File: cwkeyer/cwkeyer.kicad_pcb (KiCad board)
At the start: 2 copper layers, 19 x 17.8 mm, 7 parts, among them J1 Conn_01x05, J2 Conn_01x03, Q1 S8050, U1 ATtiny85-20SU

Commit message: Change R1 from 1K to 4.7K
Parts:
- R1: value 1K -> 4.7K
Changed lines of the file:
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@@
       (effects (font (size 1 1) (thickness 0.15)))
     )
-    (fp_text value 1K (at 0 1.65 90) (layer F.Fab)
+    (fp_text value 4.7K (at 0 1.65 90) (layer F.Fab)
       (effects (font (size 1 1) (thickness 0.15)))
     )

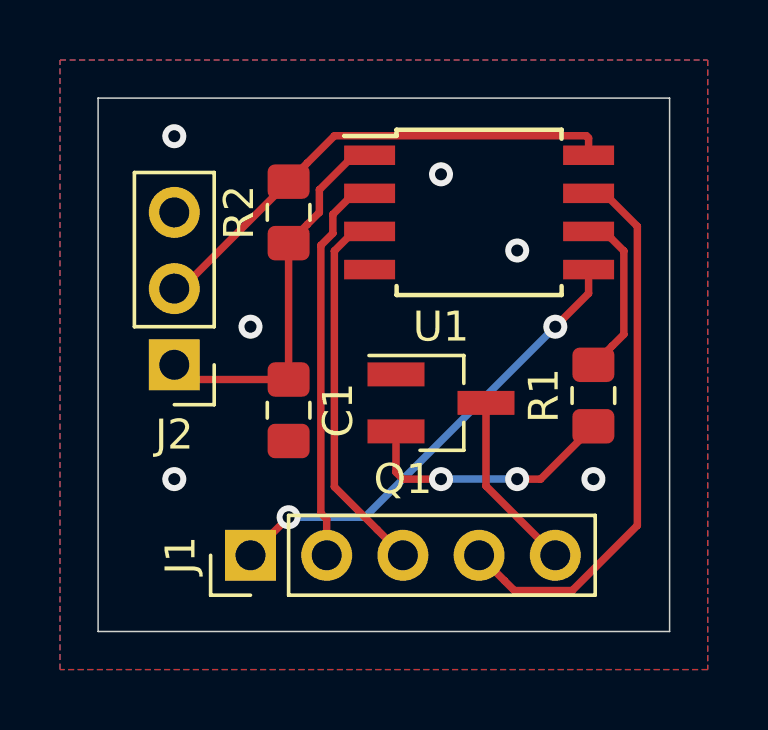
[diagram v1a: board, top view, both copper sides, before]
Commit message: Add C2 between VCC and GND. Reroute the PCB.
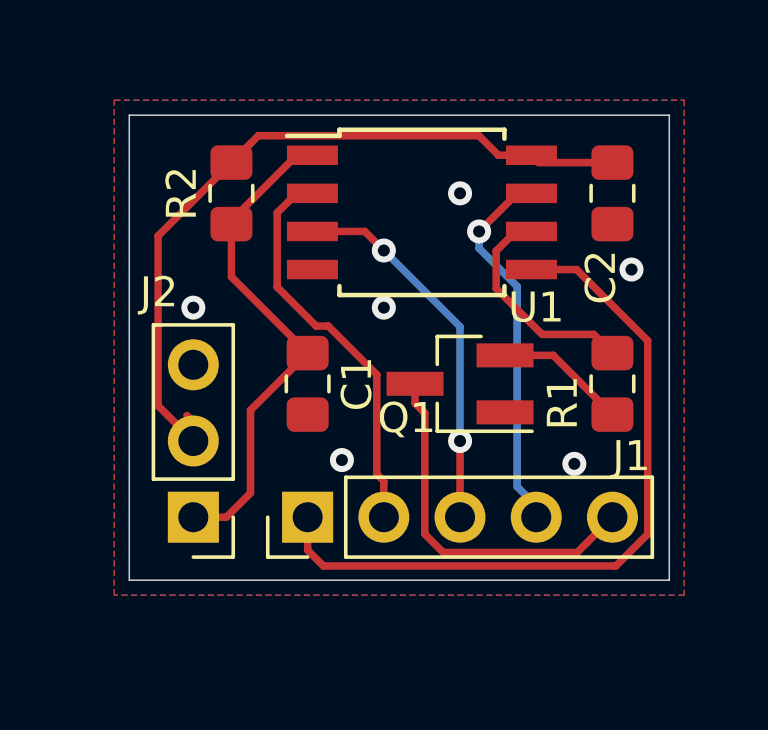
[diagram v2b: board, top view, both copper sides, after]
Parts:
- added C2: 10u, Capacitor_SMD:C_0805_2012Metric_Pad1.15x1.40mm_HandSolder, F.Cu at (141.6, 78.1)
- moved J2 5.12 mm to (127.6, 88.9)
- moved J1 2.29 mm to (131.4, 88.9)
- moved R2 2.01 mm to (128.9, 78.1)
- moved U1 1.91 mm to (135.3, 78.7)
- moved C1 1.09 mm to (131.4, 84.5)
- moved Q1 0.90 mm to (136.5, 84.5), turned to 180 degrees
- moved R1 0.75 mm to (141.6, 84.5)
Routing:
- net VCC: track 16.5 -> 25.4 mm
- net SW: track 15.7 -> 24.4 mm, vias 2 -> 0
- net TONE: track 18.7 -> 12.6 mm, vias 0 -> 1
- net KEY: track 6.04 -> 12.1 mm
- net Net-(Q1-Pad2): track 8.76 -> 4.40 mm, vias 2 -> 0
- net RESET: track 12.9 -> 16.8 mm
- net Net-(R1-Pad2): track 5.66 -> 7.46 mm
- net PAD_R: track 12.5 -> 12.6 mm, vias 0 -> 2
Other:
- board size 19 x 17.8 mm -> 18 x 15.5 mm
